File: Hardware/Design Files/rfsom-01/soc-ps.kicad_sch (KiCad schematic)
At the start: 4 parts

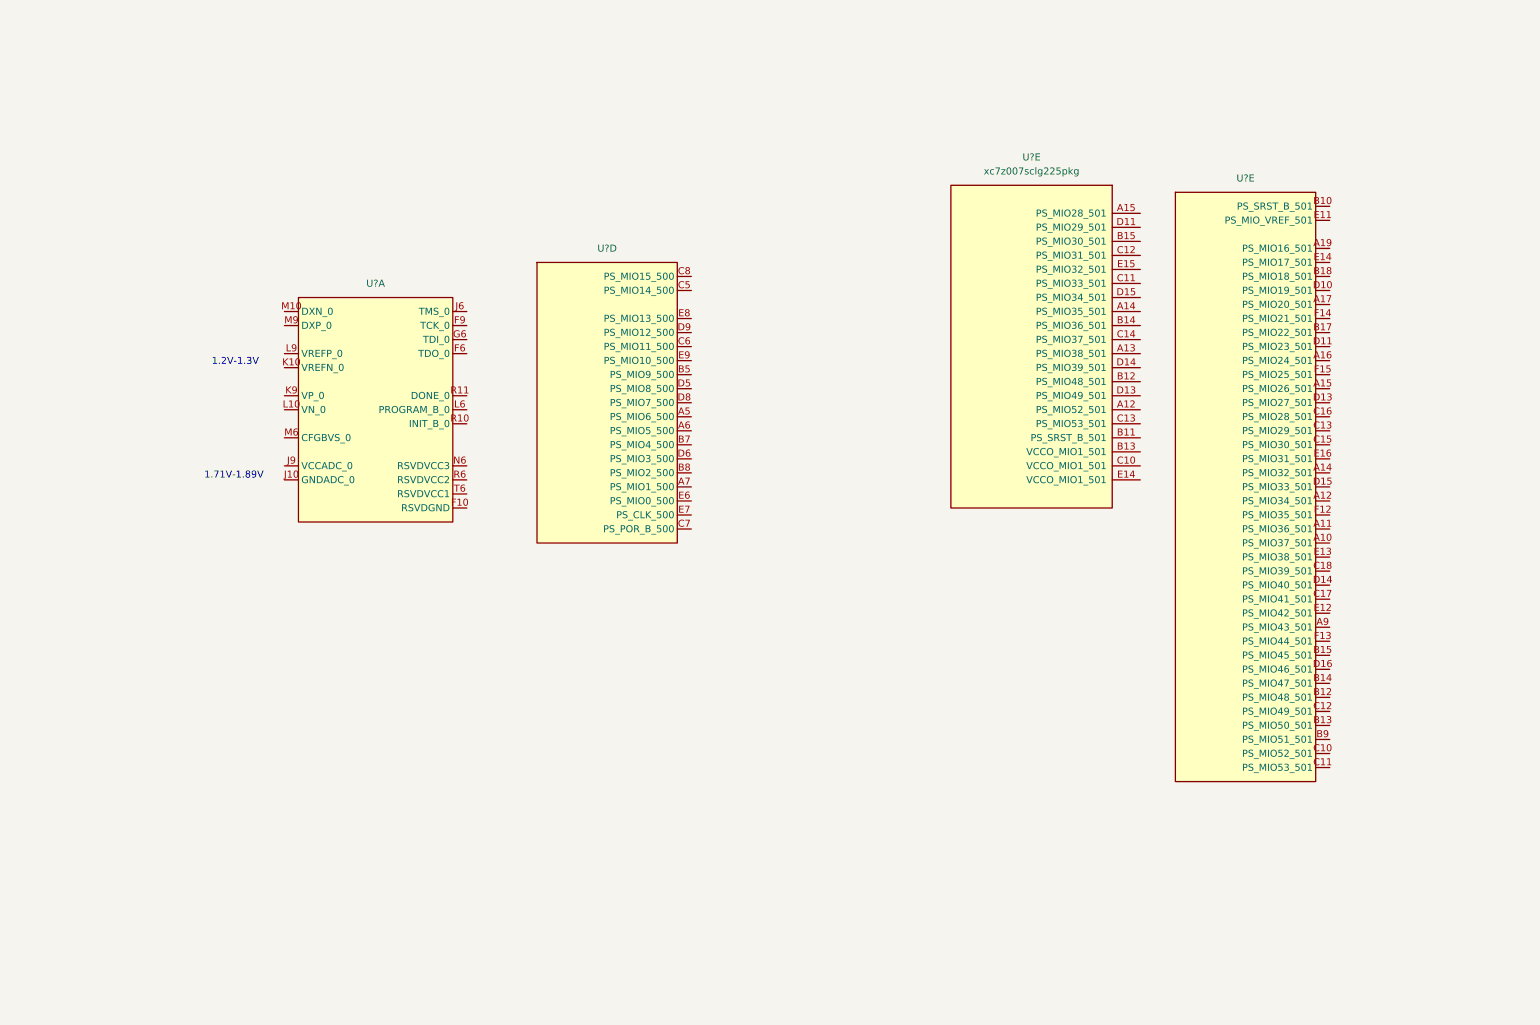
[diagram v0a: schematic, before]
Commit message: ddr progress; added more conns;
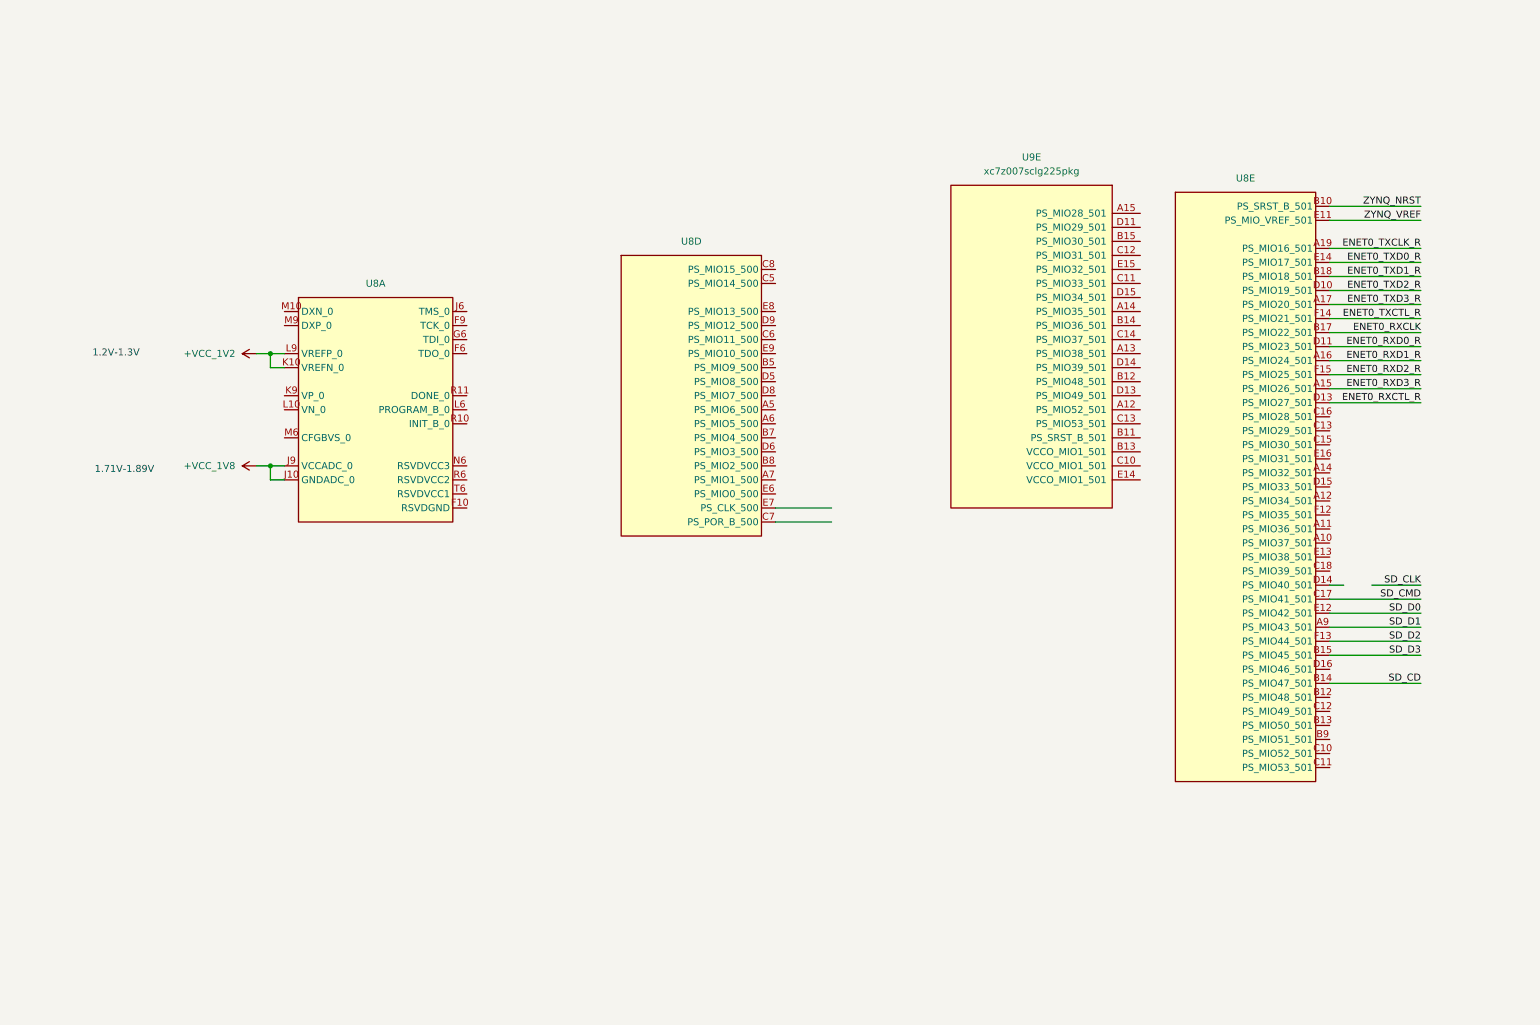
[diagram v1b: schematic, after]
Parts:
- U8: renamed from U?; footprint Package_BGA:Xilinx_CLG400 -> ICs:CLG400
- gave numbers to parts that had none: 1
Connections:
- net +VCC_1V8: now reaches U8.J10 (GNDADC_0)
- net +VCC_1V8: now also U8.J9 (VCCADC_0)
- net +VCC_1V2: now reaches U8.K10 (VREFN_0)
- net +VCC_1V2: now also U8.L9 (VREFP_0)
- net ENET0_RXD3_R: now reaches U8.A15 (PS_MIO26_501)
- net ENET0_RXD1_R: now reaches U8.A16 (PS_MIO24_501)
- net ENET0_TXD3_R: now reaches U8.A17 (PS_MIO20_501)
- net ENET0_TXCLK_R: now reaches U8.A19 (PS_MIO16_501)
- net SD_D1: now reaches U8.A9 (PS_MIO43_501)
- net ZYNQ_NRST: now reaches U8.B10 (PS_SRST_B_501)
- net SD_CD: now reaches U8.B14 (PS_MIO47_501)
- net SD_D3: now reaches U8.B15 (PS_MIO45_501)
- net ENET0_RXCLK: now reaches U8.B17 (PS_MIO22_501)
- net ENET0_TXD1_R: now reaches U8.B18 (PS_MIO18_501)
- net SD_CMD: now reaches U8.C17 (PS_MIO41_501)
- net ENET0_TXD2_R: now reaches U8.D10 (PS_MIO19_501)
- net ENET0_RXD0_R: now reaches U8.D11 (PS_MIO23_501)
- net ENET0_RXCTL_R: now reaches U8.D13 (PS_MIO27_501)
- net ZYNQ_VREF: now reaches U8.E11 (PS_MIO_VREF_501)
- net SD_D0: now reaches U8.E12 (PS_MIO42_501)
- net ENET0_TXD0_R: now reaches U8.E14 (PS_MIO17_501)
- net SD_D2: now reaches U8.F13 (PS_MIO44_501)
- net ENET0_TXCTL_R: now reaches U8.F14 (PS_MIO21_501)
- net ENET0_RXD2_R: now reaches U8.F15 (PS_MIO25_501)
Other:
- moved on the sheet: U8D

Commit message: ps progress; added ftdi; mezz pinout pedinging;
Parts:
- added C?: GRM188R70J474KA01D, Capacitor_SMD:C_0603_1608Metric, symbol Capacitors:GRM188R70J474KA01D
- added C? (x5): CL05B104KA5NNNC, Capacitor_SMD:C_0402_1005Metric_Pad0.74x0.62mm_HandSolder, symbol Capacitors:CL05B104KA5NNNC
- added C?: CL10B105KA8NNNC, Capacitor_SMD:C_0603_1608Metric_Pad1.08x0.95mm_HandSolder, symbol Capacitors:CL10B105KA8NNNC
- added D?: 150060BS75000, LED_SMD:LED_0603_1608Metric_Pad1.05x0.95mm_HandSolder, symbol Diodes:150060BS75000
- added D?: ESD204DQAR, Diodes:USON-10, symbol Diodes:ESD204DQAR
- added FB? (x2): MPZ1608S601ATA00, Resistor_SMD:R_0603_1608Metric, symbol Inductors:MPZ1608S601ATA00
- added J? (x3): ~, Jumper:SolderJumper-2_P1.3mm_Open_RoundedPad1.0x1.5mm, symbol Miscellaneous:JMP_SLD
- added J?: DM3CS-SF, Connectors:DM3CS-SF, symbol Connectors:DM3CS-SF
- added R? (x2): RC0603JR-070RL, Resistor_SMD:R_0603_1608Metric_Pad0.98x0.95mm_HandSolder, symbol Resistors:RC0603JR-070RL
- added R?: RT0402FRE0740R2L, Resistor_SMD:R_0402_1005Metric, symbol Resistors:RT0402FRE0740R2L
- added R?: RC0603FR-07220RL, Resistor_SMD:R_0603_1608Metric_Pad0.98x0.95mm_HandSolder, symbol Resistors:RC0603FR-07220RL
- added R? (x3): RC0603FR-071KL, Resistor_SMD:R_0603_1608Metric_Pad0.98x0.95mm_HandSolder, symbol Resistors:RC0603FR-071KL
- added R? (x2): RC0603FR-0747K5L, Resistor_SMD:R_0603_1608Metric_Pad0.98x0.95mm_HandSolder, symbol Resistors:RC0603FR-0747K5L
- added R? (x4): RC0402FR-07100RL, Resistor_SMD:R_0603_1608Metric, symbol Resistors:RC0402FR-07100RL
- added R? (x2): RES_01, Resistor_SMD:R_0402_1005Metric, symbol Resistors:RC0402FR-074K7L
- added S?: 435441019830, Miscellaneous:435441019830, symbol Miscellaneous:435441019830
- added S?: 219-3LPST, Miscellaneous:219-3LPST, symbol Miscellaneous:219-3LPST
- added TP? (x4): ~, TestPoint:TestPoint_Pad_D1.0mm, symbol Miscellaneous:TEST_POINT
- added U?: TXS02612RTWR, ICs:QFN-24-1EP_4x4mm_P0.5mm, symbol ICs:TXS02612RTWR
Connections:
- net +VCC_1V8: now also C?.1, C?.1, FB?.1, J?.2, R?.1, U?.5 (VCCA); no longer U8.J10 (GNDADC_0), U8.J9 (VCCADC_0)
- net SD_CD: now also J?.2, J?.2, R?.2
- net SD_CLK: now also R?.2, U?.9 (CLKA)
- net SD_CMD: now also U?.4 (CMDA)
- net SD_D0: now also U?.6 (DAT0A)
- net SD_D1: now also U?.7 (DAT1A)
- net SD_D2: now also U?.1 (DAT2A)
- net SD_D3: now also U?.3 (DAT3A)
- net GND: now reaches U8.F10 (RSVDGND)
- net GND: now also U8.M10 (DXN_0), U8.M9 (DXP_0), C?.2, C?.2, C?.2, C?.2, D?.3 (GND), D?.8 (GND), FB?.1, J?.6 (VSS), J?.S1, J?.S2, J?.S3, J?.S4, R?.1, R?.2, R?.2, R?.2, R?.2, S?.2, S?.4, U?.11 (GND), U?.2 (GND), U?.25 (EP)
- net JTAG_TDO_R: now reaches U8.F6 (TDO_0)
- net JTAG_TDO_R: now also R?.2
- net JTAG_TCK_R: now reaches U8.F9 (TCK_0)
- net JTAG_TCK_R: now also R?.2
- net JTAG_TDI_R: now reaches U8.G6 (TDI_0)
- net JTAG_TDI_R: now also R?.2
- net JTAG_TMS_R: now reaches U8.J6 (TMS_0)
- net JTAG_TMS_R: now also R?.2
- net VADC+: now reaches U8.K9 (VP_0)
- net VADC+: now also U8.J9 (VCCADC_0), C?.1, C?.1, C?.1, FB?.2, R?.2
- net VADC-: now reaches U8.L10 (VN_0)
- net VADC-: now also U8.J10 (GNDADC_0), C?.2, C?.2, C?.2, FB?.2, R?.2
- net at U8.L6 (PROGRAM_B_0): now also R?.1, S?.1, S?.3
- net +VCC_3V3: now reaches U8.M6 (CFGBVS_0)
- net +VCC_3V3: now also U8.N6 (RSVDVCC3), U8.R6 (RSVDVCC2), U8.T6 (RSVDVCC1), C?.1, C?.1, J?.4 (VDD), R?.2, R?.2, S?.4, S?.5, S?.6, U?.17 (VCC_B1), U?.21 (VCC_B0)
- net at U8.R10 (INIT_B_0): now also R?.1
- net at U8.R11 (DONE_0): now also D?.2 (A)
- net at U8.D14 (PS_MIO40_501): now also R?.1
- new net: J?.1, J?.9 (CD)
- new net: D?.1 (K), R?.2
- new net: R?.1, S?.2
- new net: R?.1, S?.3
- new net: J?.8 (DAT1), U?.16 (DAT1_B0)
- new net: J?.7 (DAT0), U?.18 (DAT0_B0)
- new net: J?.5 (CLK), U?.19 (CLK_B0)
- new net: J?.3 (CMD), U?.20 (CMD_B0)
- new net: J?.2 (DAT3), U?.22 (DAT3_B0)
- new net: J?.1 (DAT2), U?.23 (DAT2_B0)
- new net: D?.6 (NC), R?.1
- new net: D?.9 (NC), R?.1
- new net: R?.1, S?.1
- new net: D?.7 (NC), R?.1
- new net: D?.10 (NC), R?.1
- new net EXT_SD_CD: J?.1
- new net EXT_SD_CLK: U?.13 (CLK_B1)
- new net EXT_SD_CMD: U?.12 (CMD_B1)
- new net EXT_SD_D0: U?.14 (DAT0_B1)
- new net EXT_SD_D1: U?.15 (DAT1_B1)
- new net EXT_SD_D2: U?.8 (DAT2_B1)
- new net EXT_SD_D3: U?.10 (DAT3_B1)
- new net EXT_VADC+: R?.1
- new net EXT_VADC-: R?.1
- new net JTAG_TCK: D?.4 (IO3), TP?.1
- new net JTAG_TDI: D?.2 (IO2), TP?.1
- new net JTAG_TDO: D?.1 (IO1), TP?.1
- new net JTAG_TMS: D?.5 (IO4), TP?.1
- new net SD_SEL: J?.1, R?.1, U?.24 (SEL)
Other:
- note removed: "1.2V-1.3V"
- note removed: "1.71V-1.89V"
- moved on the sheet: U8A, U8D

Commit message: some ddr routing progress; layerstack per pcbway standard options, review reqd; commit prior to ddr split;
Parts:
- removed U9: xc7z007sclg225pkg, Zynq7000:CLG225, symbol ICs:xc7z007sclg225pkg
- added R53, R54, R55, R56, R57, R58, R59: RC0603FR-0720KL, Resistor_SMD:R_0201_0603Metric, symbol Resistors:RC0603FR-0720KL
- added R63, R66, R67: RC0603FR-0710KL, Resistor_SMD:R_0603_1608Metric, symbol Resistors:RC0603FR-0710KL
- added R64: RC0603FR-07220RL, Resistor_SMD:R_0603_1608Metric, symbol Resistors:RC0603FR-07220RL
- added S3: 435441019830, Miscellaneous:435441019830, symbol Miscellaneous:435441019830
- C104: renamed from C?; footprint Capacitor_SMD:C_0603_1608Metric_Pad1.08x0.95mm_HandSolder -> Capacitor_SMD:C_0603_1608Metric
- C105, C107, C108, C109, C110: renamed from C?; footprint Capacitor_SMD:C_0402_1005Metric_Pad0.74x0.62mm_HandSolder -> Capacitor_SMD:C_0402_1005Metric
- D4: renamed from D?; footprint LED_SMD:LED_0603_1608Metric_Pad1.05x0.95mm_HandSolder -> LED_SMD:LED_0603_1608Metric
- R42, R43, R44, R49, R52, R60, R61, R62: renamed from R?; footprint Resistor_SMD:R_0603_1608Metric_Pad0.98x0.95mm_HandSolder -> Resistor_SMD:R_0603_1608Metric
- gave numbers to parts that had none: 22
- renumbered U8 to U5
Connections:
- net +VCC_1V8: now also R63.1, R66.1
- net +VCC_3V3: now also R53.1
- net GND: now also R54.1, R58.1, R59.1, R67.2, S3.2, S3.4
- net ZYNQ_NRST: now also R63.2, R64.1
- net at R61.1, S2.2: now also R56.1
- net at R62.1, S2.3: now also R57.1
- net ENET0_MDC: now reaches U5.C10 (PS_MIO52_501)
- net ENET0_MDIO: now reaches U5.C11 (PS_MIO53_501)
- net ENET0_SYSCLK: now reaches U5.E16 (PS_MIO31_501)
- net MODE4: now reaches U5.A5 (PS_MIO6_500)
- net MODE4: now also R59.2
- net MODE0: now reaches U5.A6 (PS_MIO5_500)
- net MODE0: now also R55.2
- net ~{ETH_RST}: now reaches U5.B5 (PS_MIO9_500)
- net MODE2: now reaches U5.B7 (PS_MIO4_500)
- net MODE2: now also R57.2
- net MODE3: now reaches U5.B8 (PS_MIO2_500)
- net MODE3: now also R58.2
- net ZYNQ_UART_RXD: now reaches U5.C5 (PS_MIO14_500)
- net USBH_OE: now reaches U5.C6 (PS_MIO11_500)
- net ZYNQ_UART_TXD: now reaches U5.C8 (PS_MIO15_500)
- net VCFG1: now reaches U5.D5 (PS_MIO8_500)
- net VCFG1: now also R53.2
- net MODE1: now reaches U5.D6 (PS_MIO3_500)
- net MODE1: now also R56.2
- net VCFG0: now reaches U5.D8 (PS_MIO7_500)
- net VCFG0: now also R54.2
- net ETH_INIT: now reaches U5.E9 (PS_MIO10_500)
- net at R60.1, S2.1: now also R55.1
- net ZYNQ_VREF renamed RGMII_VREF
- net RGMII_VREF: now also R66.2, R67.1
- new net: R64.2, S3.1, S3.3
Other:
- moved on the sheet: R60, R61, R62, R65, S2, U5D, U5E

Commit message: added starage, usb sch; more design progress in sch;
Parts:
- removed C105, C109, C110: CL05B104KA5NNNC, Capacitor_SMD:C_0402_1005Metric, symbol Capacitors:CL05B104KA5NNNC
- removed J6, J7, J8: ~, Jumper:SolderJumper-2_P1.3mm_Open_RoundedPad1.0x1.5mm, symbol Miscellaneous:JMP_SLD
- removed J9: DM3CS-SF, Connectors:DM3CS-SF, symbol Connectors:DM3CS-SF
- removed R44, R52: RC0603FR-0747K5L, Resistor_SMD:R_0603_1608Metric, symbol Resistors:RC0603FR-0747K5L
- removed U7: TXS02612RTWR, ICs:QFN-24-1EP_4x4mm_P0.5mm, symbol ICs:TXS02612RTWR
- added C7: CL05B104KA5NNNC, Capacitor_SMD:C_0402_1005Metric, symbol Capacitors:CL05B104KA5NNNC
- added Y1: ECS-2033-500-BN, Miscellaneous:ECS-2033, symbol Miscellaneous:ECS-2033-500-BN
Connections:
- net +VCC_3V3: now also C7.1, Y1.1 (EN), Y1.4 (VDD)
- net ENET0_SYSCLK: no longer U5.E16 (PS_MIO31_501)
- net ETH_INIT: no longer U5.E9 (PS_MIO10_500)
- net GND: now also C7.2, Y1.2 (GND)
- net JTAG_TCK: now also D3.7 (NC), R47.1
- net JTAG_TDI: now also D3.9 (NC), R46.1
- net JTAG_TDO: now also D3.10 (NC), R45.1
- net JTAG_TMS: now also D3.6 (NC), R48.1
- net ~{ETH_RST}: now also U5.B13 (PS_MIO50_501); no longer U5.B5 (PS_MIO9_500)
- net ZYNQ_DONE_0: now reaches D4.2 (A), U5.R11 (DONE_0)
- net USB0_DATA5: now reaches U5.A10 (PS_MIO37_501)
- net USB0_CLK: now reaches U5.A11 (PS_MIO36_501)
- net USB0_DATA2: now reaches U5.A12 (PS_MIO34_501)
- net USB0_DATA0: now reaches U5.A14 (PS_MIO32_501)
- net SD0_CD: now reaches U5.B12 (PS_MIO48_501)
- net ~{USB_RST}: now reaches U5.B9 (PS_MIO51_501)
- net USB0_DIR: now reaches U5.C13 (PS_MIO29_501)
- net USB0_STP: now reaches U5.C15 (PS_MIO30_501)
- net USB0_DATA4: now reaches U5.C16 (PS_MIO28_501)
- net USB0_DATA7: now reaches U5.C18 (PS_MIO39_501)
- net USB0_DATA1: now reaches U5.D15 (PS_MIO33_501)
- net ZYNQ_UART0_RXD: now reaches U5.D16 (PS_MIO46_501)
- net USB0_DATA6: now reaches U5.E13 (PS_MIO38_501)
- net USB0_DATA3: now reaches U5.F12 (PS_MIO35_501)
- net ~{QSPI_CS}: now reaches U5.A7 (PS_MIO1_500)
- net ~{PS_POR}: now reaches U5.C7 (PS_POR_B_500)
- net SD1_CLK: now reaches U5.D9 (PS_MIO12_500)
- net PS_CLK_50M: now reaches U5.E7 (PS_CLK_500)
- net PS_CLK_50M: now also Y1.3 (OUT)
- net SD1_D1: now reaches U5.E8 (PS_MIO13_500)
- net MODE0 renamed QSPI_DQ3/MIO5
- net MODE1 renamed QSPI_DQ1/MIO3
- net MODE2 renamed QSPI_DQ2/MIO4
- net MODE3 renamed QSPI_DQ0/MIO2
- net MODE4 renamed QSPI_CLK/MIO6
- net SD_CD renamed ZYNQ_UART0_TXD
- net SD_CLK renamed SD0_CLK
- net SD_CMD renamed SD0_CMD
- net SD_D0 renamed SD0_D0
- net SD_D1 renamed SD0_D1
- net SD_D2 renamed SD0_D2
- net SD_D3 renamed SD0_D3
- net USBH_OE renamed SD1_CMD
- net VCFG0 renamed MIO7
- net VCFG1 renamed MIO8
- net ZYNQ_UART_RXD renamed SD1_D2
- net ZYNQ_UART_TXD renamed SD1_D3
- new net SD1_D0: U5.E9 (PS_MIO10_500)
- new net USB0_NXT: U5.E16 (PS_MIO31_501)
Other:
- note added: "!"
- note added: "Bank 0 - 2.5V/3.3V Bank 1 - 1.8V"
- note added: "[Cascade mode enabled] [PLL Enabled] 0 0 0 - JTAG 0 0 1 - NOR [N/A] 0 1 0 - NAND [N/A] 1 0 0 - QSPI 1 1 0 - SD Card"
- moved on the sheet: C104, C106, C107, C108, D3, D4, FB10, FB11, R42, R43, R45, R46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
